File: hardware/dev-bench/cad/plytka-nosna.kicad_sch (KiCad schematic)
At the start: 65 parts, among them J1 ARDUINO POWER, J10 CC1120EM P2, J11 ANALIZATOR, J12 VTEST 0-15V, J2 ARDUINO A0-A5, J3 ARDUINO D0-D7, J4 ARDUINO D8-SCL, J5 DEVKITC J1, J6 DEVKITC J3, J7 SHARP 4694, J8 FRAM 4719, J9 CC1120EM P1, Q1 MMBT3904, SW1 GÓRA, SW2 DÓŁ, SW3 OK, SW4 WSTECZ, SW5 CISZA, SW6 PRZYGOTOWANIE

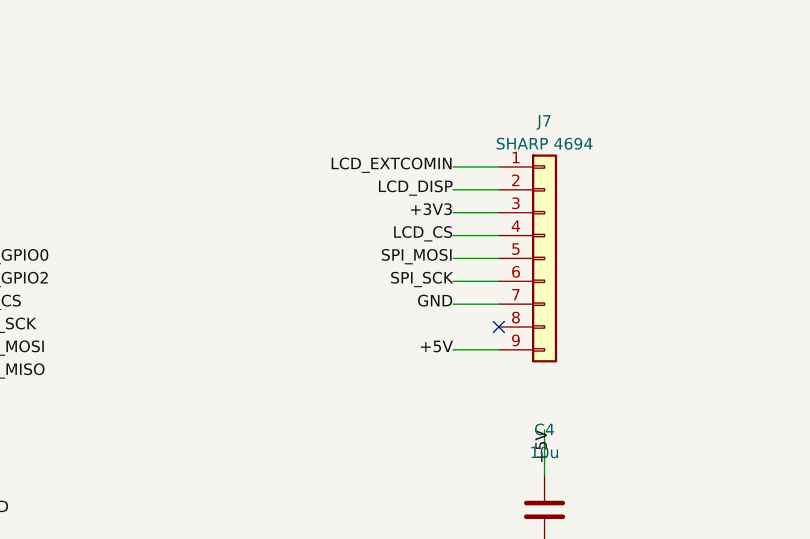
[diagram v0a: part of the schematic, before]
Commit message: Dev bench: carrier N1 after the review against manufacturers' documents (F83)
- J7: Adafruit 4694 pin order VIN..EIN with the display face up; the old
  order followed the parts-side fab print and shorted +3V3 to GND.
- JP3 moved next to J11, outside the X-NUCLEO-S2868A2 outline.
- J9/J10: Samtec TFM-110-01-L-D through-hole, the listed SFM mate
  (FTS-...-DV was an SMT part).
- Pin names on the silkscreen at J7 and J8, P20 band on the 1:1 print,
  solid GND pad J7.3.
- Fabrication package for a quote: FAB-NOTES.txt (also in the ZIP),
  English assembly BOM and SMD placement list.
- Board rerouted (Freerouting 2.5.0 needs Java 25), ERC 0, DRC 0,
  reproduction checked; pre-order list, bring-up and docs updated.

Co-Authored-By: Claude Opus 5.5 <noreply@anthropic.com>
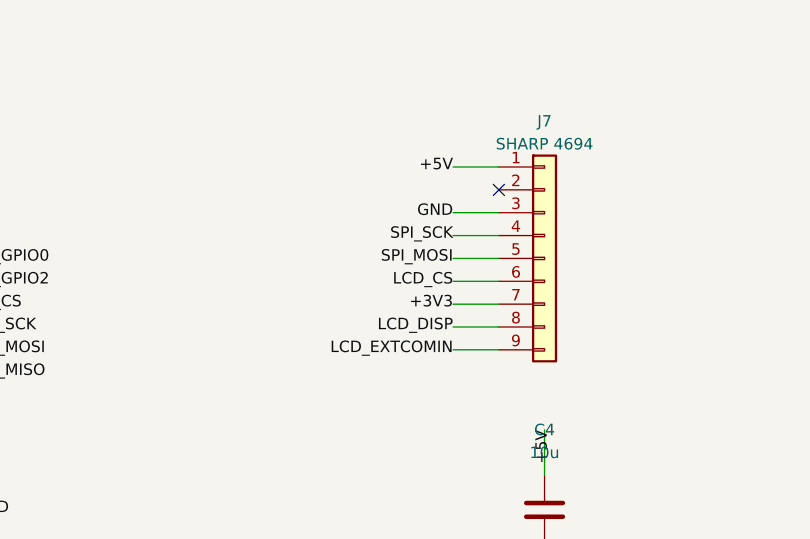
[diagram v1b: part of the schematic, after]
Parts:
- J10, J9: MPN FTS-110-01-L-DV -> TFM-110-01-L-D
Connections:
- net +3V3: now also J7.7 (Pin_7); no longer J7.3 (Pin_3)
- net +5V: now also J7.1 (Pin_1); no longer J7.9 (Pin_9)
- net GND: now also J7.3 (Pin_3); no longer J7.7 (Pin_7)
- net LCD_CS: now also J7.6 (Pin_6); no longer J7.4 (Pin_4)
- net LCD_DISP: now also J7.8 (Pin_8); no longer J7.2 (Pin_2)
- net LCD_EXTCOMIN: now also J7.9 (Pin_9); no longer J7.1 (Pin_1)
- net SPI_SCK: now also J7.4 (Pin_4); no longer J7.6 (Pin_6)
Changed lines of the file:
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@@
           (size 1.27 1.27))
         (hide yes)))
-    (property "MPN" "FTS-110-01-L-DV"
+    (property "MPN" "TFM-110-01-L-D"
       (at 182.88 48.26 0)
       (effects
@@
           (size 1.27 1.27))
         (hide yes)))
-    (property "MPN" "FTS-110-01-L-DV"
+    (property "MPN" "TFM-110-01-L-D"
       (at 182.88 86.36 0)
       (effects
@@
       (type default))
 )
-  (label "LCD_EXTCOMIN"
+  (label "+5V"
     (at 248.92 38.1 180)
     (effects
@@
       (justify right))
 )
-  (wire
-    (pts
-      (xy 254.0 40.64)
-      (xy 248.92 40.64))
-    (stroke
-      (width 0)
-      (type default))
-)
-  (label "LCD_DISP"
-    (at 248.92 40.64 180)
-    (effects
-      (font
-        (size 1.27 1.27))
-      (justify right))
+  (no_connect
+    (at 254.0 40.64)
 )
   (wire
@@
       (type default))
 )
-  (label "+3V3"
+  (label "GND"
     (at 248.92 43.18 180)
     (effects
@@
       (type default))
 )
-  (label "LCD_CS"
+  (label "SPI_SCK"
     (at 248.92 45.72 180)
     (effects
@@
       (type default))
 )
-  (label "SPI_SCK"
+  (label "LCD_CS"
     (at 248.92 50.8 180)
     (effects
@@
       (type default))
 )
-  (label "GND"
+  (label "+3V3"
     (at 248.92 53.34 180)
     (effects
@@
       (justify right))
 )
-  (no_connect
-    (at 254.0 55.88)
+  (wire
+    (pts
+      (xy 254.0 55.88)
+      (xy 248.92 55.88))
+    (stroke
+      (width 0)
+      (type default))
+)
+  (label "LCD_DISP"
+    (at 248.92 55.88 180)
+    (effects
+      (font
+        (size 1.27 1.27))
+      (justify right))
 )
   (wire
@@
       (type default))
 )
-  (label "+5V"
+  (label "LCD_EXTCOMIN"
     (at 248.92 58.42 180)
     (effects

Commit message: Dev bench N1: fabrication package after fab and assembler review
Fab and assembly house view of the N1 package: paste layer in the
Gerbers, 10 uF capacitor as CL21A106KAYNNNE (taped), HAL lead-free
finish in job.gbrjob, copper 0.3 mm from holes (DRC rule), silk lines
0.15 mm, assembler BOM with SMD parts only, title block on montaz.pdf,
FAB-NOTES with the stated tolerances and assembly scope.

Docs after the final orientation check: P20 band is copper-free on
B.Cu with no vias, P5 notch margin about 0.55 mm on the J11 side,
full list of parts under the X-NUCLEO, DK J2 USB plug under J6 in the
fit check, TFM mated height with SFM-02 to be measured.

Board regenerated with the kept routing session; ERC 0, DRC 0.

Co-Authored-By: Claude Opus 5.5 <noreply@anthropic.com>
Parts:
- C1, C4: MPN CL21A106KAYNNNC -> CL21A106KAYNNNE
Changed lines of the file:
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@@
           (size 1.27 1.27))
         (hide yes)))
-    (property "MPN" "CL21A106KAYNNNC"
+    (property "MPN" "CL21A106KAYNNNE"
       (at 182.88 137.16 0)
       (effects
@@
           (size 1.27 1.27))
         (hide yes)))
-    (property "MPN" "CL21A106KAYNNNC"
-      (at 259.08 76.2 0)
-      (effects
+    (property "MPN" "CL21A106KAYNNNE"
+      (at 259.08 76.2 0)
+      (effects

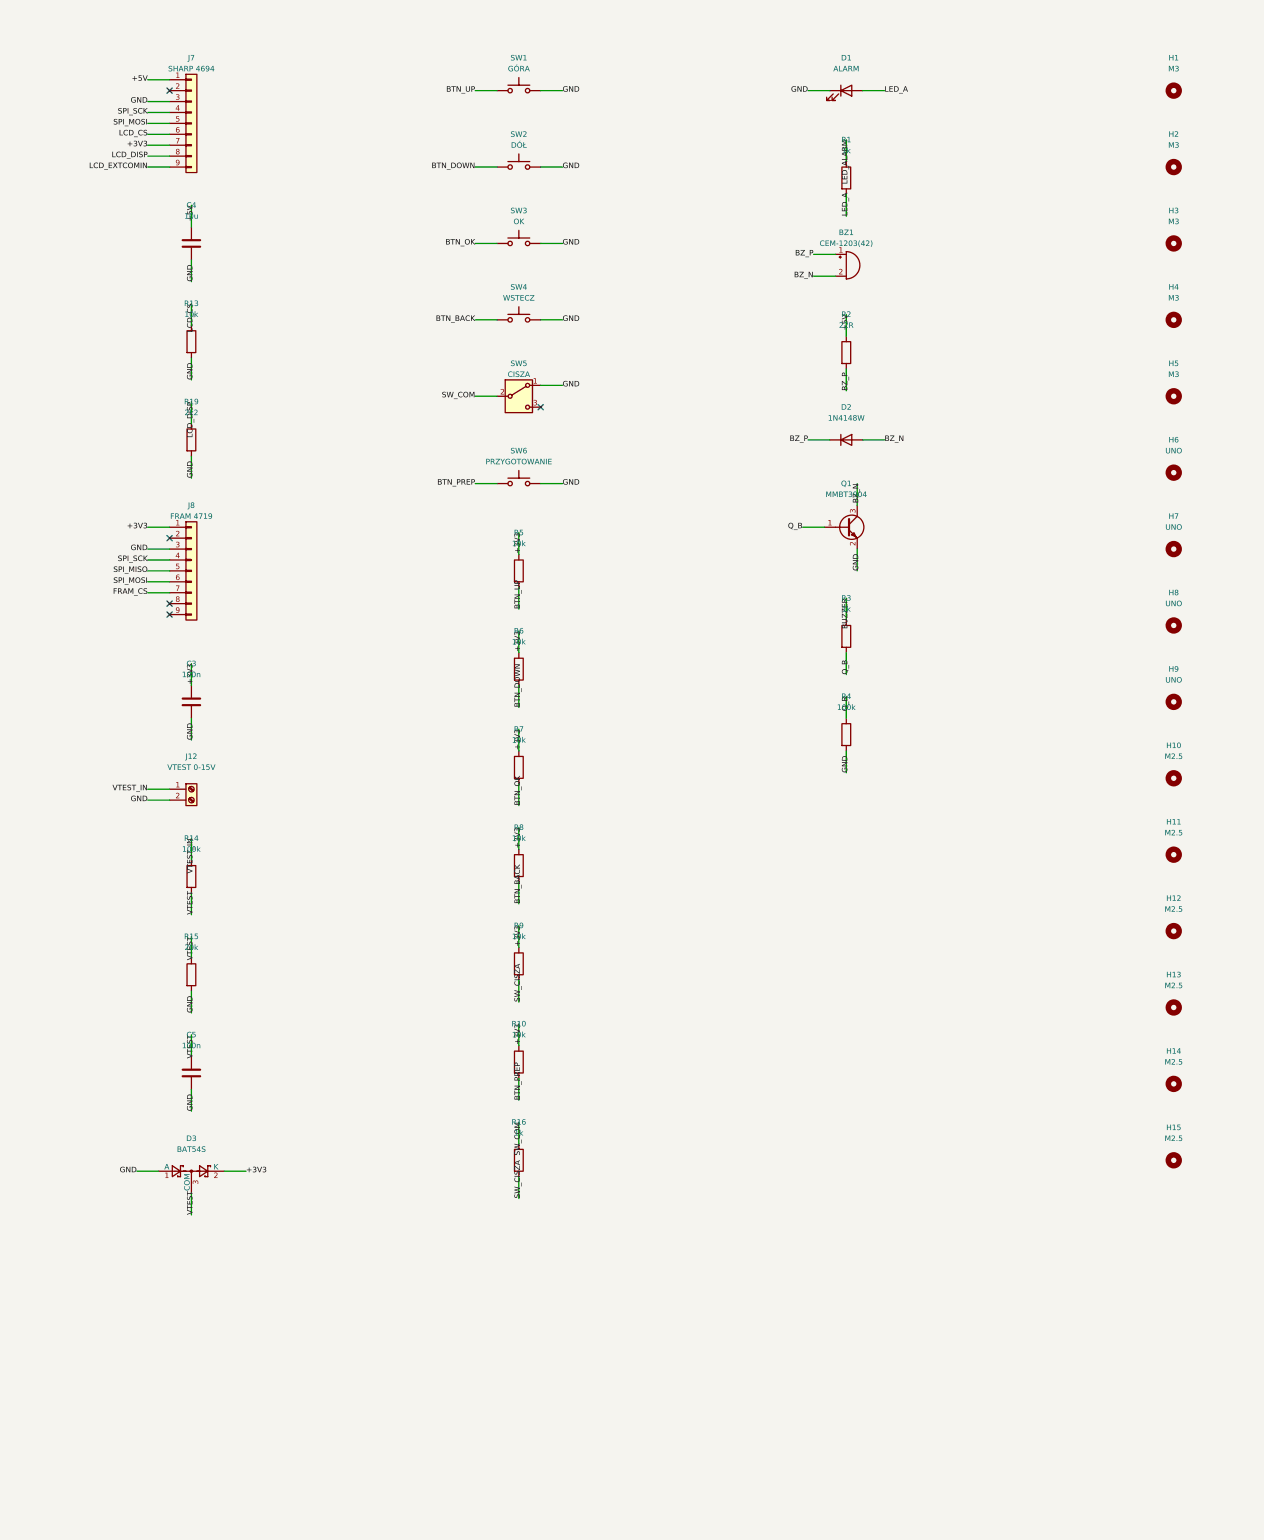
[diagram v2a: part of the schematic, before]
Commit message: Dev bench N1: production FRAM and Sharp panel on the board (F86)
The Adafruit 4719 FRAM board is out of stock until 2027 and both Adafruit
boards come from a single vendor, so the bench could not be built and did
not exercise the parts the station will use. N1 now carries them directly:

- FRAM U1 in SOIC-8: Infineon CY15B104QN-50SXI or RAMXEED MB85RS4MTPF,
  with 10 kOhm CS pull-up; WP and HOLD/RESET tied to 3.3 V.
- Sharp LS027B7DH01A panel on 0.8 mm foam tape over the board, in a
  Hirose FH12-10S-0.5SH FPC connector (J7) powered from the 5 V rail,
  with the capacitors the Sharp datasheet recommends; generator asserts
  nothing sits under the panel.
- Samtec SSQ stacking sockets for J1-J4 instead of the Adafruit 85 kit.
- Firmware recognises CY15B104QN (C2 2C) and rejects 1.8 V variants.

Rerouted (Freerouting 2.5.0, 0 unrouted), ERC/DRC 0, reproduction
identical. Docs, BOM, cost and bring-up updated; open: panel supply on
bench B (DevKitC 5V pin 4.6-4.8 V vs 4.8 V minimum), J7 position at fit
check.

Co-Authored-By: Claude Opus 5.5 <noreply@anthropic.com>
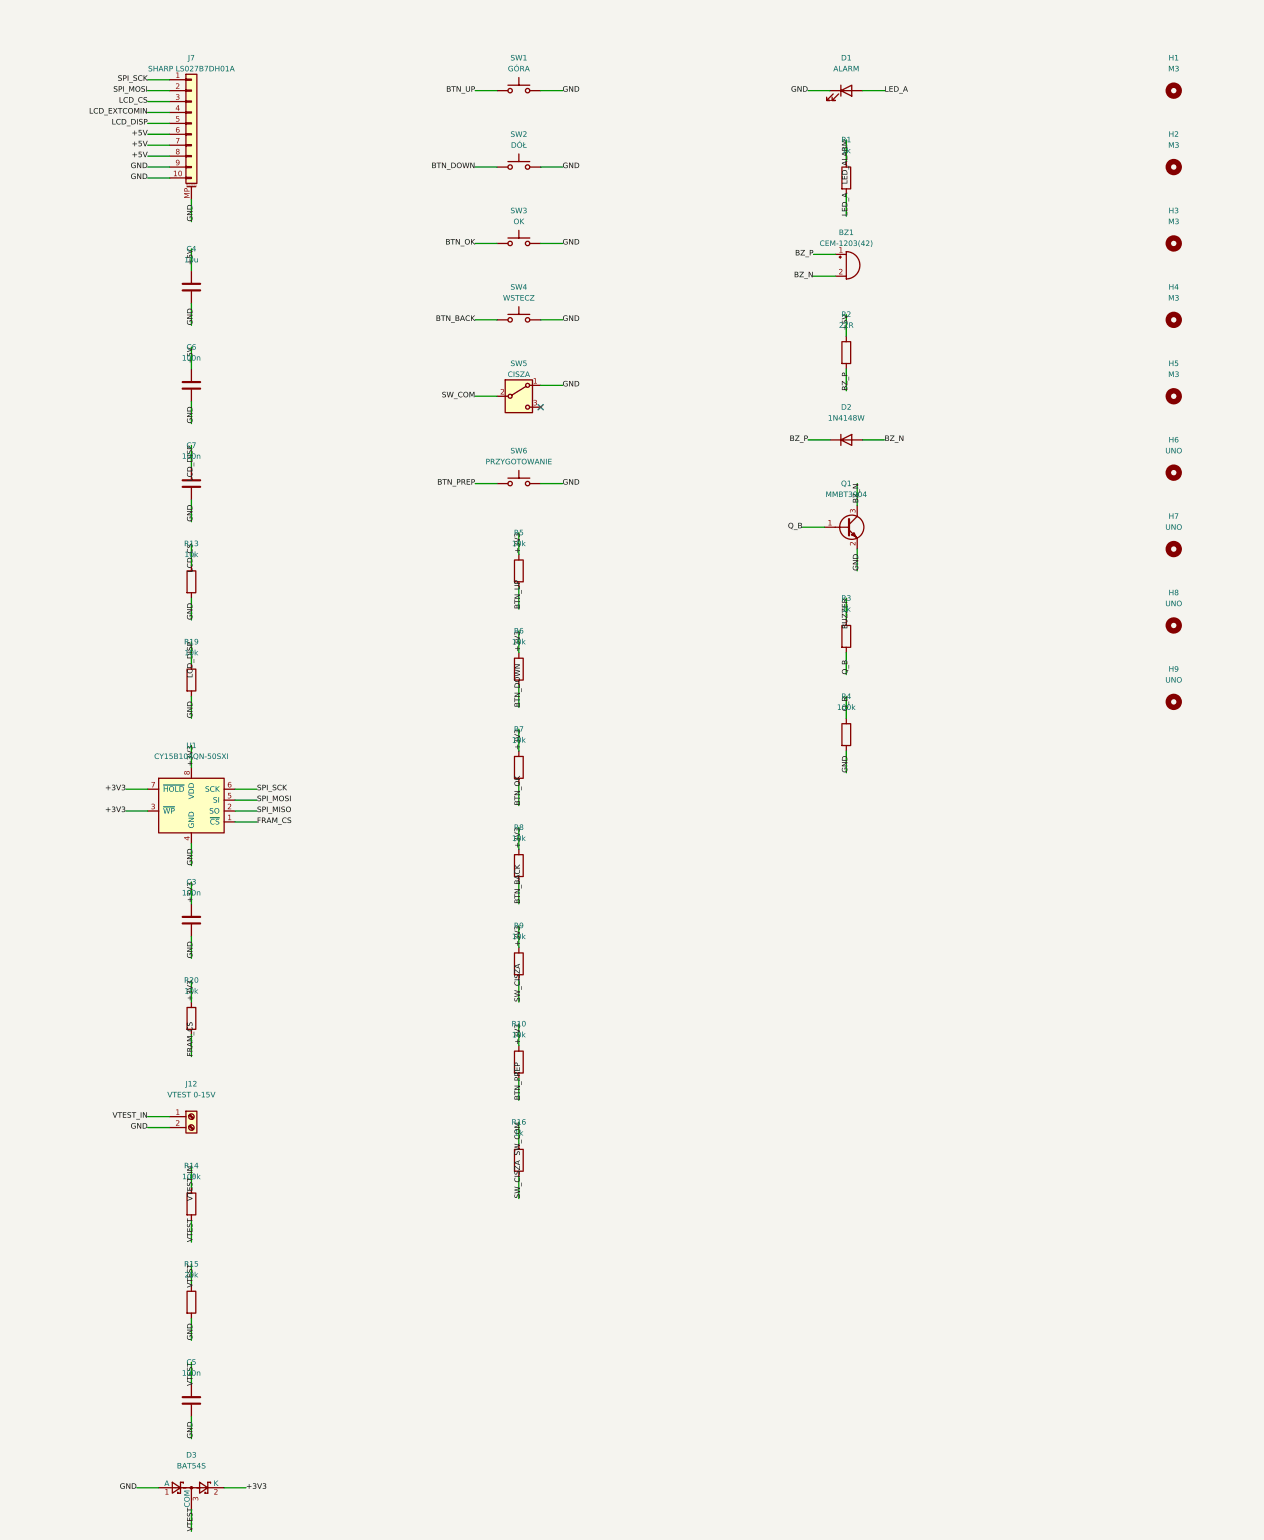
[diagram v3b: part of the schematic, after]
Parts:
- removed H10, H11, H12, H13, H14, H15: M2.5, MountingHole:MountingHole_2.7mm_M2.5, symbol Mechanical:MountingHole
- removed J8: FRAM 4719, Connector_PinSocket_2.54mm:PinSocket_1x09_P2.54mm_Vertical, symbol Connector_Generic:Conn_01x09
- added C6, C7: 100n, Capacitor_SMD:C_0805_2012Metric, symbol Device:C
- added R20: 10k, Resistor_SMD:R_0805_2012Metric, symbol Device:R
- added U1: CY15B104QN-50SXI, Package_SO:SOIC-8_5.3x5.3mm_P1.27mm, symbol Memory_NVRAM:MB85RS2MT
- J1, J3: MPN Adafruit 85 -> SSQ-108-03-T-S; Manufacturer Adafruit -> Samtec
- J2: MPN Adafruit 85 -> SSQ-106-03-T-S; Manufacturer Adafruit -> Samtec
- J4: MPN Adafruit 85 -> SSQ-110-03-T-S; Manufacturer Adafruit -> Samtec
- J7: value SHARP 4694 -> SHARP LS027B7DH01A; footprint Connector_PinSocket_2.54mm:PinSocket_1x09_P2.54mm_Vertical -> Connector_FFC-FPC:Hirose_FH12-10S-0.5SH_1x10-1MP_P0.50mm_Horizontal; symbol Connector_Generic:Conn_01x09 -> Connector_Generic_MountingPin:Conn_01x10_MountingPin; MPN PPTC091LFBN-RC -> FH12-10S-0.5SH(55); Manufacturer Sullins -> Hirose
- R19: value 2k2 -> 10k; MPN RC0805FR-072K2L -> RC0805FR-0710KL
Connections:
- net +3V3: now also R20.1, U1.3 (~{WP}), U1.7 (~{HOLD}), U1.8 (VDD); no longer J7.7 (Pin_7)
- net +5V: now also J7.6 (Pin_6), J7.7 (Pin_7), J7.8 (Pin_8), C6.1; no longer J7.1 (Pin_1)
- net FRAM_CS: now also R20.2, U1.1 (~{CS})
- net GND: now also J7.10 (Pin_10), J7.9 (Pin_9), J7.MP (MountPin), C6.2, C7.2, U1.4 (GND); no longer J7.3 (Pin_3)
- net LCD_CS: now also J7.3 (Pin_3); no longer J7.6 (Pin_6)
- net LCD_DISP: now also J7.5 (Pin_5), C7.1; no longer J7.8 (Pin_8)
- net LCD_EXTCOMIN: now also J7.4 (Pin_4); no longer J7.9 (Pin_9)
- net SPI_MISO: now also U1.2 (SO)
- net SPI_MOSI: now also J7.2 (Pin_2), U1.5 (SI); no longer J7.5 (Pin_5)
- net SPI_SCK: now also J7.1 (Pin_1), U1.6 (SCK); no longer J7.4 (Pin_4)
- no-connect marks 52 -> 48
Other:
- moved on the sheet: C3, C4, C5, D3, J12, R13, R14, R15, R19

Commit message: Dev bench N1: panel boost, EXTCOMIN failure handling, audit fixes (F103)
Update the N1 carrier to the current specification and the N1 audit:
- panel VDD/VDDA from an MCP1640 boost (+5V_LCD, 4.90-5.36 V worst
  case) on both benches; Adafruit 4694 rejected as unavailable
- firmware keeps DISP low and reports a fault when the EXTCOMIN timer
  fails (no software VCOM with EXTMODE=H); FRAM SPI at 8 MHz
- VTEST divider from 0.1% resistors with two-point calibration;
  oscilloscope procedure for J7, radio and FRAM; J7 continuity by pin
  group; ammeter drop check while transmitting
- DRC rules file was silently ignored by kicad-cli; fixed syntax and
  added a canary rule; export refuses to run unless ERC/DRC are clean
- board comparison covers zone fills, fields and attributes
- panel datasheet LCP-1112041; part availability checked 2026-10-08
  (10 uF caps to CL21A106KAYNNNG, DevKitC N8R8 only)

Co-Authored-By: Claude Opus 5.5 <noreply@anthropic.com>
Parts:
- added C10: 100p, Capacitor_SMD:C_0805_2012Metric, symbol Device:C
- added C8, C9: 10u, Capacitor_SMD:C_0805_2012Metric, symbol Device:C
- added L1: 4u7, Inductor_SMD:L_Wuerth_WE-TPC-3816, symbol Device:L
- added R21: 1M, Resistor_SMD:R_0805_2012Metric, symbol Device:R
- added R22: 309k, Resistor_SMD:R_0805_2012Metric, symbol Device:R
- added U2: MCP1640, Package_TO_SOT_SMD:SOT-23-6, symbol Regulator_Switching:MCP1640x-xCHY
- C1, C4: MPN CL21A106KAYNNNE -> CL21A106KAYNNNG
- R14: MPN RC0805FR-07100KL -> RT0805BRD07100KL
- R15: MPN RC0805FR-0720KL -> RT0805BRD0720KL
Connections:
- net +3V3: now also C8.1, L1.1, U2.3 (EN), U2.6 (V_{IN})
- net +5V: no longer C4.1, C6.1, J7.6 (Pin_6), J7.7 (Pin_7), J7.8 (Pin_8)
- net GND: now also C8.2, C9.2, R22.2, U2.2 (GND)
- new net +5V_LCD: C10.1, C4.1, C6.1, C9.1, J7.6 (Pin_6), J7.7 (Pin_7), J7.8 (Pin_8), R21.1, U2.5 (V_{OUT})
- new net BST_FB: C10.2, R21.2, R22.1, U2.4 (V_{FB})
- new net BST_SW: L1.2, U2.1 (SW)
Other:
- moved on the sheet: BZ1, C3, C5, D1, D2, D3, H1, H2, H3, H4, H5, H6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
